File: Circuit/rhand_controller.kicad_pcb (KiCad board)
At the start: 2 copper layers, 100 x 100 mm, 39 parts, among them P1 BLUETOOTH, P10 LV_ADC, P11 LW_ADC, P12 RU_ADC, P13 RV_ADC, P14 RW_ADC, P2 CONN_01X06, P3 Wall, P4 CW, P5 Enable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

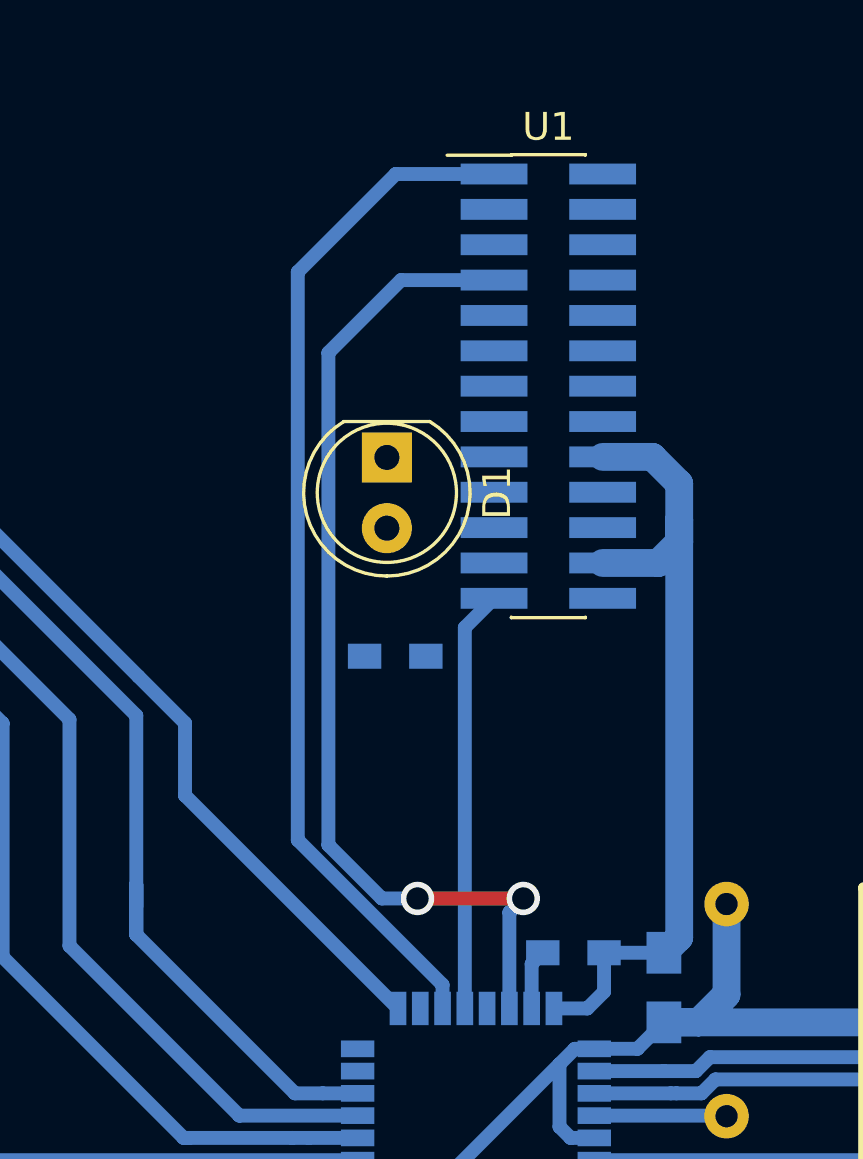
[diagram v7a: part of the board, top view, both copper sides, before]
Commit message: IM315のLEDの配線変更
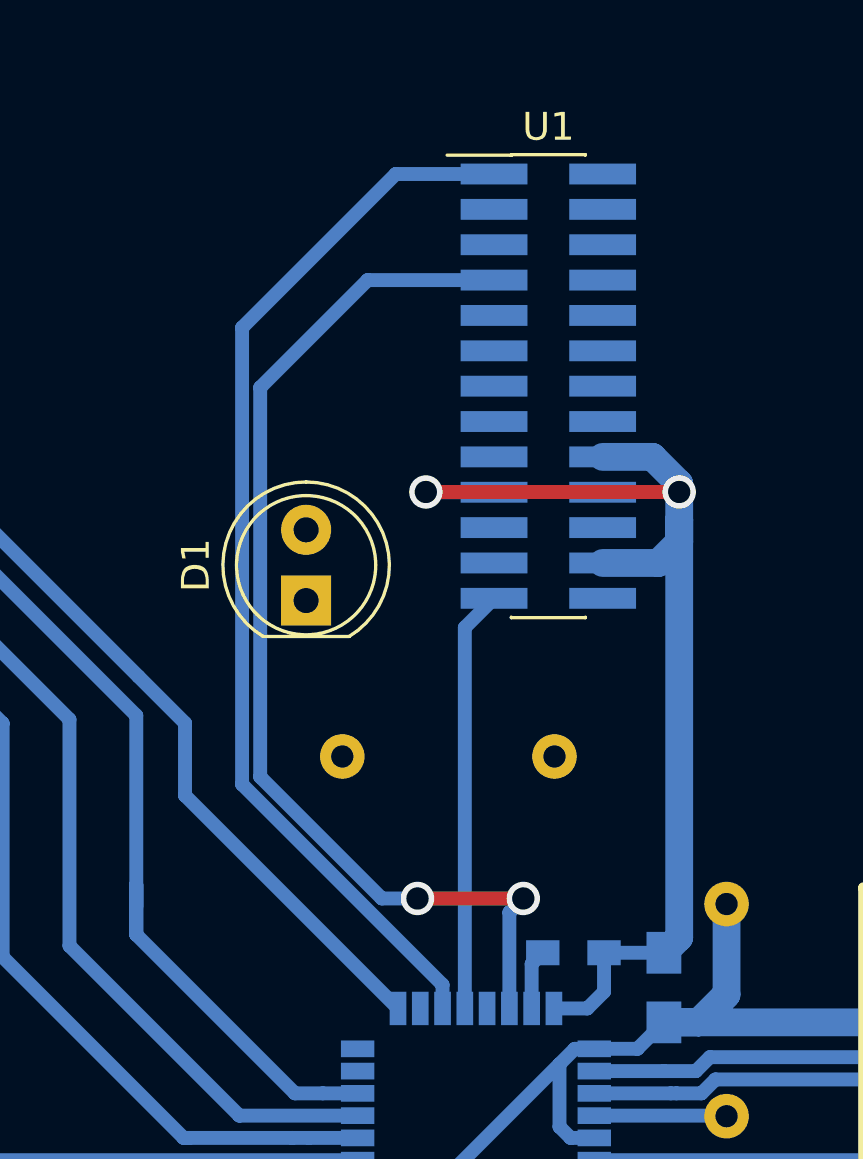
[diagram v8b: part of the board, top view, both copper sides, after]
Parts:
- R5: footprint Resistors_SMD:R_0603_HandSoldering -> Resistors_THT:R_Axial_DIN0207_L6.3mm_D2.5mm_P7.62mm_Horizontal
- moved D1 5.90 mm to (87.9, 113.6), turned to 90 degrees
- moved R5 4.07 mm to (89.2, 119.2)
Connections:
- D1 pad 1: Net-(D1-Pad1) -> GND
- R5 pad 1: Net-(D1-Pad1) -> Net-(R5-Pad1)
- R5 pad 2: GND -> Net-(D1-Pad2)
- U1 pad 21: Net-(D1-Pad2) -> Net-(R5-Pad1)
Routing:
- net GND: track 406.6 -> 418.2 mm, vias 0 -> 2
- net /315MHz_TXD: track 36.7 -> 39.4 mm
- net /busy: track 37.1 -> 38.8 mm
